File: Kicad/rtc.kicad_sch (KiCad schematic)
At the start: 8 parts, among them U801 DS1307Z+, Y801 32,768 Hz

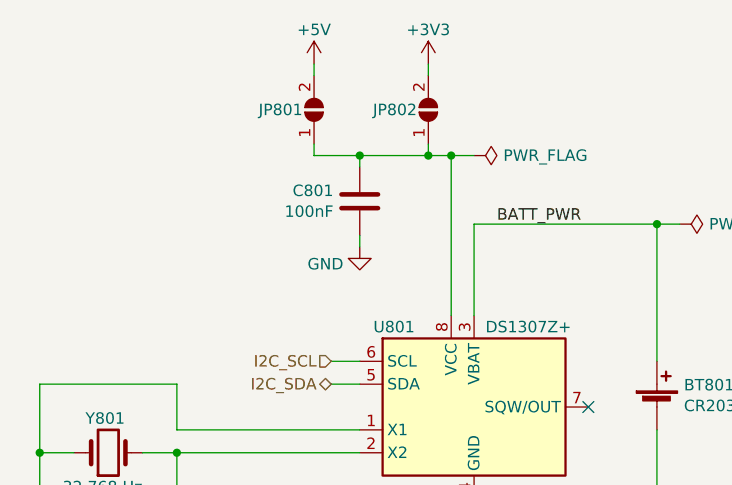
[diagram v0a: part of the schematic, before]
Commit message: Replaced decoupling caps, and worked on PCB layout.
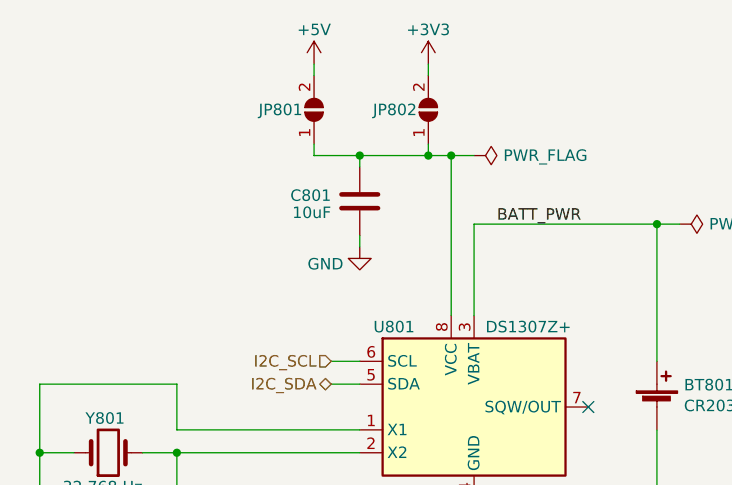
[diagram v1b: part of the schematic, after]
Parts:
- C801: value 100nF -> 10uF; LCSC Part# C49678 -> C15850; MPN CC0805KRX7R9BB104 -> CL21A106KAYNNNE; Manufacturer Yageo -> Samsung; Tolerance X7R -> X5R; Voltage 50V -> 25V
- JP801, JP802: footprint Jumper:SolderJumper-2_P1.3mm_Open_Pad1.0x1.5mm -> Jumper:SolderJumper-2_P1.3mm_Open_RoundedPad1.0x1.5mm
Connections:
- net GND: now also C801.1; no longer C801.2
- net at JP801.1 (A), JP802.1 (A), U801.8 (VCC): now also C801.2; no longer C801.1
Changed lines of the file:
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@@
     (effects (font (size 1.27 1.27)) (justify right))
-  )
-  (symbol (lib_id "Device:C") (at 124.46 68.58 0) (mirror y) (unit 1)
-    (in_bom yes) (on_board yes)
-    (property "Reference" "C801" (id 0) (at 121.539 67.4116 0)
-      (effects (font (size 1.27 1.27)) (justify left))
-    )
-    (property "Value" "100nF" (id 1) (at 121.539 69.723 0)
-      (effects (font (size 1.27 1.27)) (justify left))
-    )
-    (property "Footprint" "Capacitor_SMD:C_0805_2012Metric_Pad1.18x1.45mm_HandSolder" (id 2) (at 123.4948 72.39 0)
-      (effects (font (size 1.27 1.27)) hide)
-    )
-    (property "Datasheet" "~" (id 3) (at 124.46 68.58 0)
-      (effects (font (size 1.27 1.27)) hide)
-    )
-    (property "Manufacturer" "Yageo" (id 4) (at 303.53 153.67 0)
-      (effects (font (size 1.27 1.27)) hide)
-    )
-    (property "DNP" "0" (id 5) (at 124.46 68.58 0)
-      (effects (font (size 1.27 1.27)) hide)
-    )
-    (property "Digikey" "~" (id 6) (at 124.46 68.58 0)
-      (effects (font (size 1.27 1.27)) hide)
-    )
-    (property "MPN" "CC0805KRX7R9BB104" (id 7) (at 124.46 68.58 0)
-      (effects (font (size 1.27 1.27)) hide)
-    )
-    (property "Mouser" "~" (id 8) (at 124.46 68.58 0)
-      (effects (font (size 1.27 1.27)) hide)
-    )
-    (property "LCSC Part#" "C49678" (id 9) (at 124.46 68.58 0)
-      (effects (font (size 1.27 1.27)) hide)
-    )
-    (property "Tolerance" "X7R" (id 10) (at 124.46 68.58 0)
-      (effects (font (size 1.27 1.27)) hide)
-    )
-    (property "Voltage" "50V" (id 11) (at 124.46 68.58 0)
-      (effects (font (size 1.27 1.27)) hide)
-    )
-    (property "JLCPCB Collection" "Basic" (id 12) (at 124.46 68.58 0)
-      (effects (font (size 1.27 1.27)) hide)
-    )
-    (pin "1")
-    (pin "2")
   )
   (symbol (lib_id "power:GND") (at 124.46 73.66 0) (unit 1)
@@
       (effects (font (size 1.27 1.27)) hide)
     )
-    (property "Footprint" "Jumper:SolderJumper-2_P1.3mm_Open_Pad1.0x1.5mm" (id 2) (at 132.08 58.42 0)
+    (property "Footprint" "Jumper:SolderJumper-2_P1.3mm_Open_RoundedPad1.0x1.5mm" (id 2) (at 132.08 58.42 0)
       (effects (font (size 1.27 1.27)) hide)
     )
@@
       (effects (font (size 1.27 1.27)) hide)
     )
-    (property "Footprint" "Jumper:SolderJumper-2_P1.3mm_Open_Pad1.0x1.5mm" (id 2) (at 119.38 58.42 0)
+    (property "Footprint" "Jumper:SolderJumper-2_P1.3mm_Open_RoundedPad1.0x1.5mm" (id 2) (at 119.38 58.42 0)
       (effects (font (size 1.27 1.27)) hide)
     )
@@
       (effects (font (size 1.27 1.27)) hide)
     )
+    (pin "1")
+    (pin "2")
+  )
+  (symbol (lib_id "Device:C") (at 124.46 68.58 0) (mirror x) (unit 1)
+    (in_bom yes) (on_board yes)
+    (property "Reference" "C801" (id 0) (at 121.285 67.945 0)
+      (effects (font (size 1.27 1.27)) (justify right))
+    )
+    (property "Value" "10uF" (id 1) (at 121.285 69.85 0)
+      (effects (font (size 1.27 1.27)) (justify right))
+    )
+    (property "Footprint" "Capacitor_SMD:C_0805_2012Metric_Pad1.18x1.45mm_HandSolder" (id 2) (at 125.4252 64.77 0)
+      (effects (font (size 1.27 1.27)) hide)
+    )
+    (property "Datasheet" "~" (id 3) (at 124.46 68.58 0)
+      (effects (font (size 1.27 1.27)) hide)
+    )
+    (property "DNP" "0" (id 4) (at 124.46 68.58 0)
+      (effects (font (size 1.27 1.27)) hide)
+    )
+    (property "Digikey" "~" (id 5) (at 124.46 68.58 0)
+      (effects (font (size 1.27 1.27)) hide)
+    )
+    (property "MPN" "CL21A106KAYNNNE" (id 6) (at 124.46 68.58 0)
+      (effects (font (size 1.27 1.27)) hide)
+    )
+    (property "Manufacturer" "Samsung" (id 7) (at 124.46 68.58 0)
+      (effects (font (size 1.27 1.27)) hide)
+    )
+    (property "LCSC Part#" "C15850" (id 8) (at 124.46 68.58 0)
+      (effects (font (size 1.27 1.27)) hide)
+    )
+    (property "Tolerance" "X5R" (id 9) (at 124.46 68.58 0)
+      (effects (font (size 1.27 1.27)) hide)
+    )
+    (property "Voltage" "25V" (id 10) (at 124.46 68.58 0)
+      (effects (font (size 1.27 1.27)) hide)
+    )
+    (property "Mouser" "~" (id 11) (at 124.46 68.58 0)
+      (effects (font (size 1.27 1.27)) hide)
+    )
+    (property "JLCPCB Collection" "Basic" (id 12) (at 124.46 68.58 0)
+      (effects (font (size 1.27 1.27)) hide)
+    )

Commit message: Added source resistors on SPI bus.
Also renumbered pages.
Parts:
- renumbered BT801 to BT1201, C801 to C1201, C802 to C1202, C803 to C1203, JP801 to JP1201, JP802 to JP1202, U801 to U1201, Y801 to Y1201
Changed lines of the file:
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@@
   (symbol (lib_id "power:GND") (at 124.46 73.66 0) (unit 1)
     (in_bom yes) (on_board yes)
-    (property "Reference" "#PWR0803" (id 0) (at 124.46 80.01 0)
+    (property "Reference" "#PWR01203" (id 0) (at 124.46 80.01 0)
       (effects (font (size 1.27 1.27)) hide)
     )
@@
   (symbol (lib_id "power:+3V3") (at 132.08 53.34 0) (unit 1)
     (in_bom yes) (on_board yes)
-    (property "Reference" "#PWR0802" (id 0) (at 132.08 57.15 0)
+    (property "Reference" "#PWR01202" (id 0) (at 132.08 57.15 0)
       (effects (font (size 1.27 1.27)) hide)
     )
@@
   (symbol (lib_id "power:GND") (at 137.16 111.76 0) (unit 1)
     (in_bom yes) (on_board yes)
-    (property "Reference" "#PWR0806" (id 0) (at 137.16 118.11 0)
+    (property "Reference" "#PWR01206" (id 0) (at 137.16 118.11 0)
       (effects (font (size 1.27 1.27)) hide)
     )
@@
   (symbol (lib_id "Device:Crystal") (at 96.52 96.52 0) (mirror x) (unit 1)
     (in_bom yes) (on_board yes)
-    (property "Reference" "Y801" (id 0) (at 93.98 92.71 0)
+    (property "Reference" "Y1201" (id 0) (at 93.98 92.71 0)
       (effects (font (size 1.27 1.27)) (justify left))
     )
@@
   (symbol (lib_id "power:GND") (at 157.48 111.76 0) (unit 1)
     (in_bom yes) (on_board yes)
-    (property "Reference" "#PWR0807" (id 0) (at 157.48 118.11 0)
+    (property "Reference" "#PWR01207" (id 0) (at 157.48 118.11 0)
       (effects (font (size 1.27 1.27)) hide)
     )
@@
   (symbol (lib_id "Device:Battery_Cell") (at 157.48 91.44 0) (unit 1)
     (in_bom yes) (on_board yes)
-    (property "Reference" "BT801" (id 0) (at 160.4772 89.0016 0)
+    (property "Reference" "BT1201" (id 0) (at 160.4772 89.0016 0)
       (effects (font (size 1.27 1.27)) (justify left))
     )
@@
   (symbol (lib_id "power:PWR_FLAG") (at 160.02 71.12 270) (unit 1)
     (in_bom yes) (on_board yes)
-    (property "Reference" "#FLG0802" (id 0) (at 161.925 71.12 0)
+    (property "Reference" "#FLG01202" (id 0) (at 161.925 71.12 0)
       (effects (font (size 1.27 1.27)) hide)
     )
@@
   (symbol (lib_id "Device:C") (at 88.9 105.41 0) (unit 1)
     (in_bom yes) (on_board yes)
-    (property "Reference" "C802" (id 0) (at 91.821 104.2416 0)
+    (property "Reference" "C1202" (id 0) (at 91.821 104.2416 0)
       (effects (font (size 1.27 1.27)) (justify left))
     )
@@
   (symbol (lib_id "power:+5V") (at 119.38 53.34 0) (unit 1)
     (in_bom yes) (on_board yes)
-    (property "Reference" "#PWR0801" (id 0) (at 119.38 57.15 0)
+    (property "Reference" "#PWR01201" (id 0) (at 119.38 57.15 0)
       (effects (font (size 1.27 1.27)) hide)
     )
@@
   (symbol (lib_id "power:GND") (at 104.14 111.76 0) (unit 1)
     (in_bom yes) (on_board yes)
-    (property "Reference" "#PWR0805" (id 0) (at 104.14 118.11 0)
+    (property "Reference" "#PWR01205" (id 0) (at 104.14 118.11 0)
       (effects (font (size 1.27 1.27)) hide)
     )
@@
   (symbol (lib_id "Jumper:SolderJumper_2_Open") (at 132.08 58.42 90) (unit 1)
     (in_bom yes) (on_board yes)
-    (property "Reference" "JP802" (id 0) (at 130.81 58.42 90)
+    (property "Reference" "JP1202" (id 0) (at 130.81 58.42 90)
       (effects (font (size 1.27 1.27)) (justify left))
     )
@@
   (symbol (lib_id "power:PWR_FLAG") (at 137.16 63.5 270) (unit 1)
     (in_bom yes) (on_board yes)
-    (property "Reference" "#FLG0801" (id 0) (at 139.065 63.5 0)
+    (property "Reference" "#FLG01201" (id 0) (at 139.065 63.5 0)
       (effects (font (size 1.27 1.27)) hide)
     )
@@
   (symbol (lib_id "Jumper:SolderJumper_2_Open") (at 119.38 58.42 90) (unit 1)
     (in_bom yes) (on_board yes)
-    (property "Reference" "JP801" (id 0) (at 118.11 58.42 90)
+    (property "Reference" "JP1201" (id 0) (at 118.11 58.42 90)
       (effects (font (size 1.27 1.27)) (justify left))
     )
@@
   (symbol (lib_id "power:GND") (at 88.9 111.76 0) (unit 1)
     (in_bom yes) (on_board yes)
-    (property "Reference" "#PWR0804" (id 0) (at 88.9 118.11 0)
+    (property "Reference" "#PWR01204" (id 0) (at 88.9 118.11 0)
       (effects (font (size 1.27 1.27)) hide)
     )
@@
   (symbol (lib_id "Device:C") (at 104.14 105.41 0) (unit 1)
     (in_bom yes) (on_board yes)
-    (property "Reference" "C803" (id 0) (at 107.061 104.2416 0)
+    (property "Reference" "C1203" (id 0) (at 107.061 104.2416 0)
       (effects (font (size 1.27 1.27)) (justify left))
     )
@@
   (symbol (lib_id "Device:C") (at 124.46 68.58 0) (mirror x) (unit 1)
     (in_bom yes) (on_board yes)
-    (property "Reference" "C801" (id 0) (at 121.285 67.945 0)
+    (property "Reference" "C1201" (id 0) (at 121.285 67.945 0)
       (effects (font (size 1.27 1.27)) (justify right))
     )
@@
   (symbol (lib_id "Timer_RTC:DS1307Z+") (at 137.16 91.44 0) (unit 1)
     (in_bom yes) (on_board yes)
-    (property "Reference" "U801" (id 0) (at 128.27 82.55 0))
+    (property "Reference" "U1201" (id 0) (at 128.27 82.55 0))
     (property "Value" "DS1307Z+" (id 1) (at 138.43 82.55 0)
       (effects (font (size 1.27 1.27)) (justify left))

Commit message: Label adjustments.
Swap 10uF to 10u (the F is implied)
Adjust some left/right alignment and nudge some labels around
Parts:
- C1201: value 10uF -> 10u
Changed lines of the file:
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@@
       (effects (font (size 1.27 1.27)) (justify right))
     )
-    (property "Value" "10uF" (id 1) (at 121.285 69.85 0)
+    (property "Value" "10u" (id 1) (at 121.285 69.85 0)
       (effects (font (size 1.27 1.27)) (justify right))
     )

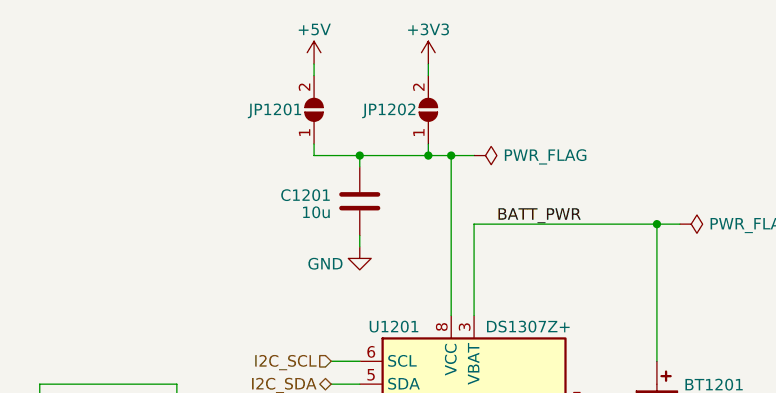
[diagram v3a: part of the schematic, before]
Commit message: Updated to KiCAD 7.
Had to move a net-tie to resolve a "too close" error.
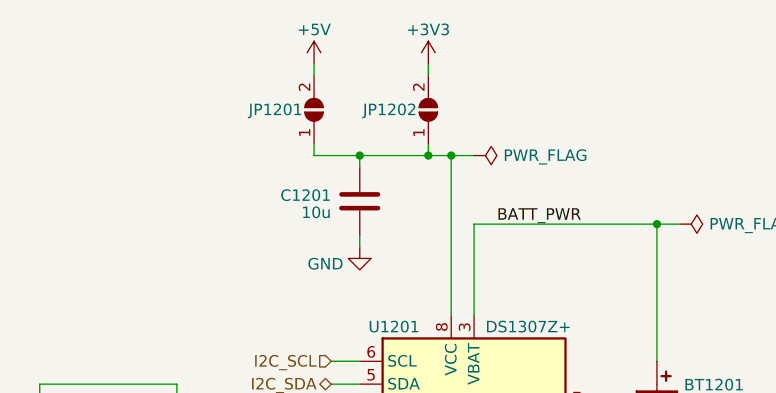
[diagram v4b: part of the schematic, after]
